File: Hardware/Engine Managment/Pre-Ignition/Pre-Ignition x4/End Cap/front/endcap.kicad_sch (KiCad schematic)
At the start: 4 parts

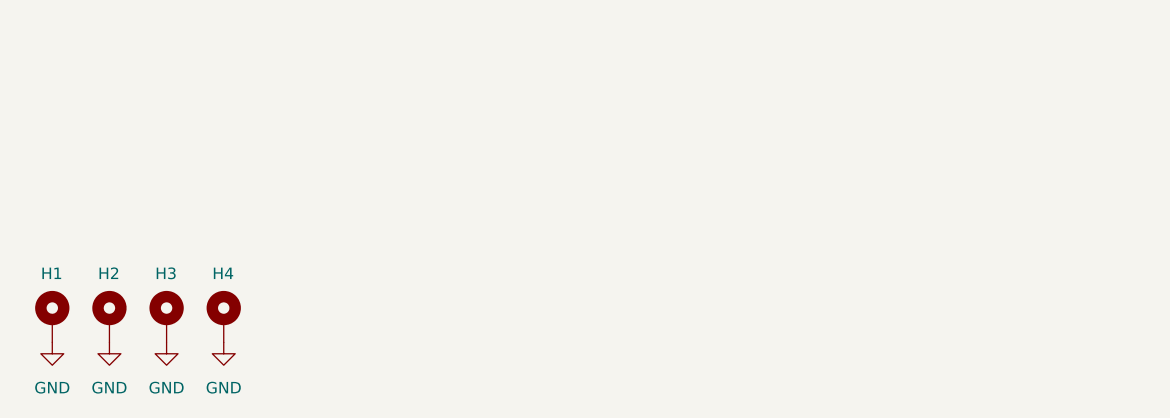
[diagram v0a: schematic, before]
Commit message: Minor updates
PMAP-M correction
Endcap updates
readme updates
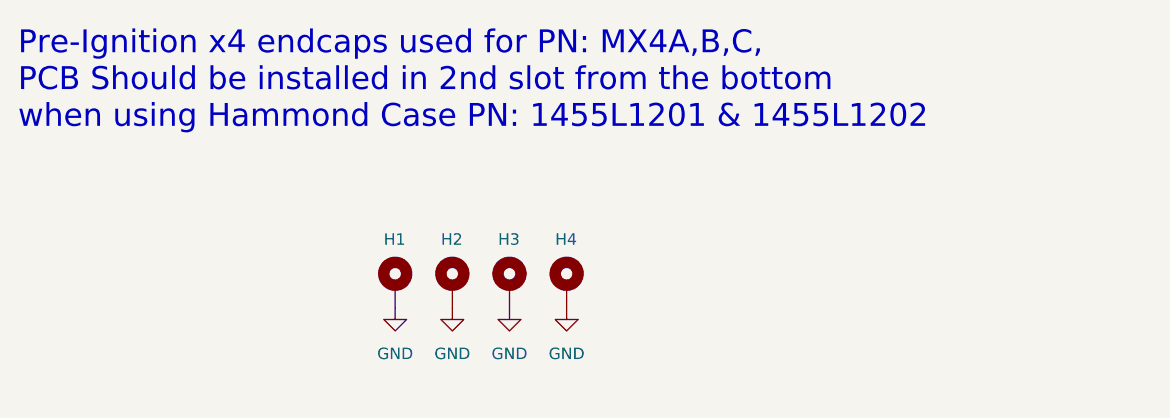
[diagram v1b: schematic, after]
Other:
- note added: "Pre-Ignition x4 endcaps used for PN: MX4A,B,C, PCB Should be installed in 2nd slot from the bottom when using Hammond Case PN: 1455L1201 & 1455L1202"
- moved on the sheet: H1, H2, H3, H4
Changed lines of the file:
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@@
 (kicad_sch (version 20230121) (generator eeschema)
   (paper "A4")
-  (symbol (lib_id "power:GND") (at 137.16 109.22 0) (unit 1)
+  (title_block
+    (date "2024-02-07")
+  )
+  (text "Pre-Ignition x4 endcaps used for PN: MX4A,B,C,\nPCB Should be installed in 2nd slot from the bottom\nwhen using Hammond Case PN: 1455L1201 & 1455L1202"
+    (at 114.3 85.725 0)
+    (effects (font (size 2.54 2.54)) (justify left bottom))
+  )
+  (symbol (lib_id "power:GND") (at 175.26 105.41 0) (unit 1)
     (in_bom yes) (on_board yes) (dnp no) (fields_autoplaced)
-    (property "Reference" "#PWR04" (at 137.16 115.57 0)
+    (property "Reference" "#PWR04" (at 175.26 111.76 0)
       (effects (font (size 1.27 1.27)) hide)
     )
-    (property "Value" "GND" (at 137.16 114.3 0)
+    (property "Value" "GND" (at 175.26 110.49 0)
       (effects (font (size 1.27 1.27)))
     )
-    (property "Footprint" "" (at 137.16 109.22 0)
+    (property "Footprint" "" (at 175.26 105.41 0)
       (effects (font (size 1.27 1.27)) hide)
     )
-    (property "Datasheet" "" (at 137.16 109.22 0)
+    (property "Datasheet" "" (at 175.26 105.41 0)
       (effects (font (size 1.27 1.27)) hide)
     )
@@
         )
       )
-      (project "endcap"
-        (path "/68b81d50-e3ab-4fb4-88ac-58934bf832b1"
-          (reference "#PWR08") (unit 1)
-        )
-      )
     )
   )
-  (symbol (lib_id "Mechanical:MountingHole_Pad") (at 124.46 106.68 0) (unit 1)
+  (symbol (lib_id "Mechanical:MountingHole_Pad") (at 162.56 102.87 0) (unit 1)
     (in_bom yes) (on_board yes) (dnp no)
-    (property "Reference" "H2" (at 123.19 101.6 0)
+    (property "Reference" "H2" (at 161.29 97.79 0)
       (effects (font (size 1.27 1.27)) (justify left))
     )
-    (property "Value" "MountingHole_Pad" (at 127 106.68 0)
+    (property "Value" "MountingHole_Pad" (at 165.1 102.87 0)
       (effects (font (size 1.27 1.27)) (justify left) hide)
     )
-    (property "Footprint" "MountingHole:MountingHole_4.3mm_M4_Pad" (at 124.46 106.68 0)
+    (property "Footprint" "MountingHole:MountingHole_4.3mm_M4_Pad" (at 162.56 102.87 0)
       (effects (font (size 1.27 1.27)) hide)
     )
-    (property "Datasheet" "~" (at 124.46 106.68 0)
+    (property "Datasheet" "~" (at 162.56 102.87 0)
       (effects (font (size 1.27 1.27)) hide)
     )
@@
         )
       )
-      (project "endcap"
-        (path "/68b81d50-e3ab-4fb4-88ac-58934bf832b1"
-          (reference "H6") (unit 1)
-        )
-      )
     )
   )
-  (symbol (lib_id "power:GND") (at 130.81 109.22 0) (unit 1)
+  (symbol (lib_id "power:GND") (at 168.91 105.41 0) (unit 1)
     (in_bom yes) (on_board yes) (dnp no) (fields_autoplaced)
-    (property "Reference" "#PWR03" (at 130.81 115.57 0)
+    (property "Reference" "#PWR03" (at 168.91 111.76 0)
       (effects (font (size 1.27 1.27)) hide)
     )
-    (property "Value" "GND" (at 130.81 114.3 0)
+    (property "Value" "GND" (at 168.91 110.49 0)
       (effects (font (size 1.27 1.27)))
     )
-    (property "Footprint" "" (at 130.81 109.22 0)
+    (property "Footprint" "" (at 168.91 105.41 0)
       (effects (font (size 1.27 1.27)) hide)
     )
-    (property "Datasheet" "" (at 130.81 109.22 0)
+    (property "Datasheet" "" (at 168.91 105.41 0)
       (effects (font (size 1.27 1.27)) hide)
     )
@@
         )
       )
-      (project "endcap"
-        (path "/68b81d50-e3ab-4fb4-88ac-58934bf832b1"
-          (reference "#PWR07") (unit 1)
-        )
-      )
     )
   )
-  (symbol (lib_id "Mechanical:MountingHole_Pad") (at 118.11 106.68 0) (unit 1)
+  (symbol (lib_id "Mechanical:MountingHole_Pad") (at 156.21 102.87 0) (unit 1)
     (in_bom yes) (on_board yes) (dnp no)
-    (property "Reference" "H1" (at 116.84 101.6 0)
+    (property "Reference" "H1" (at 154.94 97.79 0)
       (effects (font (size 1.27 1.27)) (justify left))
     )
-    (property "Value" "MountingHole_Pad" (at 120.65 106.68 0)
+    (property "Value" "MountingHole_Pad" (at 158.75 102.87 0)
       (effects (font (size 1.27 1.27)) (justify left) hide)
     )
-    (property "Footprint" "MountingHole:MountingHole_4.3mm_M4_Pad" (at 118.11 106.68 0)
+    (property "Footprint" "MountingHole:MountingHole_4.3mm_M4_Pad" (at 156.21 102.87 0)
       (effects (font (size 1.27 1.27)) hide)
     )
-    (property "Datasheet" "~" (at 118.11 106.68 0)
+    (property "Datasheet" "~" (at 156.21 102.87 0)
       (effects (font (size 1.27 1.27)) hide)
     )
@@
         )
       )
-      (project "endcap"
-        (path "/68b81d50-e3ab-4fb4-88ac-58934bf832b1"
-          (reference "H5") (unit 1)
-        )
-      )
     )
   )
-  (symbol (lib_id "Mechanical:MountingHole_Pad") (at 137.16 106.68 0) (unit 1)
+  (symbol (lib_id "Mechanical:MountingHole_Pad") (at 175.26 102.87 0) (unit 1)
     (in_bom yes) (on_board yes) (dnp no)
-    (property "Reference" "H4" (at 135.89 101.6 0)
+    (property "Reference" "H4" (at 173.99 97.79 0)
       (effects (font (size 1.27 1.27)) (justify left))
     )
-    (property "Value" "MountingHole_Pad" (at 139.7 106.68 0)
+    (property "Value" "MountingHole_Pad" (at 177.8 102.87 0)
       (effects (font (size 1.27 1.27)) (justify left) hide)
     )
-    (property "Footprint" "MountingHole:MountingHole_4.3mm_M4_Pad" (at 137.16 106.68 0)
+    (property "Footprint" "MountingHole:MountingHole_4.3mm_M4_Pad" (at 175.26 102.87 0)
       (effects (font (size 1.27 1.27)) hide)
     )
-    (property "Datasheet" "~" (at 137.16 106.68 0)
+    (property "Datasheet" "~" (at 175.26 102.87 0)
       (effects (font (size 1.27 1.27)) hide)
     )
@@
         )
       )
-      (project "endcap"
-        (path "/68b81d50-e3ab-4fb4-88ac-58934bf832b1"
-          (reference "H8") (unit 1)
-        )
-      )
     )
   )
-  (symbol (lib_id "power:GND") (at 118.11 109.22 0) (unit 1)
+  (symbol (lib_id "power:GND") (at 156.21 105.41 0) (unit 1)
     (in_bom yes) (on_board yes) (dnp no) (fields_autoplaced)
-    (property "Reference" "#PWR01" (at 118.11 115.57 0)
+    (property "Reference" "#PWR01" (at 156.21 111.76 0)
       (effects (font (size 1.27 1.27)) hide)
     )
-    (property "Value" "GND" (at 118.11 114.3 0)
+    (property "Value" "GND" (at 156.21 110.49 0)
       (effects (font (size 1.27 1.27)))
     )
-    (property "Footprint" "" (at 118.11 109.22 0)
+    (property "Footprint" "" (at 156.21 105.41 0)
       (effects (font (size 1.27 1.27)) hide)
     )
-    (property "Datasheet" "" (at 118.11 109.22 0)
+    (property "Datasheet" "" (at 156.21 105.41 0)
       (effects (font (size 1.27 1.27)) hide)
     )
@@
         )
       )
-      (project "endcap"
-        (path "/68b81d50-e3ab-4fb4-88ac-58934bf832b1"
-          (reference "#PWR05") (unit 1)
-        )
-      )
     )
   )
-  (symbol (lib_id "power:GND") (at 124.46 109.22 0) (unit 1)
+  (symbol (lib_id "power:GND") (at 162.56 105.41 0) (unit 1)
     (in_bom yes) (on_board yes) (dnp no) (fields_autoplaced)
-    (property "Reference" "#PWR02" (at 124.46 115.57 0)
+    (property "Reference" "#PWR02" (at 162.56 111.76 0)
       (effects (font (size 1.27 1.27)) hide)
     )
-    (property "Value" "GND" (at 124.46 114.3 0)
+    (property "Value" "GND" (at 162.56 110.49 0)
       (effects (font (size 1.27 1.27)))
     )
-    (property "Footprint" "" (at 124.46 109.22 0)
+    (property "Footprint" "" (at 162.56 105.41 0)
       (effects (font (size 1.27 1.27)) hide)
     )
-    (property "Datasheet" "" (at 124.46 109.22 0)
+    (property "Datasheet" "" (at 162.56 105.41 0)
       (effects (font (size 1.27 1.27)) hide)
     )
@@
         )
       )
-      (project "endcap"
-        (path "/68b81d50-e3ab-4fb4-88ac-58934bf832b1"
-          (reference "#PWR06") (unit 1)
-        )
-      )
     )
   )
-  (symbol (lib_id "Mechanical:MountingHole_Pad") (at 130.81 106.68 0) (unit 1)
+  (symbol (lib_id "Mechanical:MountingHole_Pad") (at 168.91 102.87 0) (unit 1)
     (in_bom yes) (on_board yes) (dnp no)
-    (property "Reference" "H3" (at 129.54 101.6 0)
+    (property "Reference" "H3" (at 167.64 97.79 0)
       (effects (font (size 1.27 1.27)) (justify left))
     )
-    (property "Value" "MountingHole_Pad" (at 133.35 106.68 0)
+    (property "Value" "MountingHole_Pad" (at 171.45 102.87 0)
       (effects (font (size 1.27 1.27)) (justify left) hide)
     )
-    (property "Footprint" "MountingHole:MountingHole_4.3mm_M4_Pad" (at 130.81 106.68 0)
+    (property "Footprint" "MountingHole:MountingHole_4.3mm_M4_Pad" (at 168.91 102.87 0)
       (effects (font (size 1.27 1.27)) hide)
     )
-    (property "Datasheet" "~" (at 130.81 106.68 0)
+    (property "Datasheet" "~" (at 168.91 102.87 0)
       (effects (font (size 1.27 1.27)) hide)
     )
@@
         )
       )
-      (project "endcap"
-        (path "/68b81d50-e3ab-4fb4-88ac-58934bf832b1"
-          (reference "H7") (unit 1)
-        )
-      )
